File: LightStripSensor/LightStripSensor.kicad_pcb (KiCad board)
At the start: 2 copper layers, 61.8 x 40 mm, 14 parts, among them J1 LED_OUT 5.5x2.1, J2 DC_IN 12V 5.5x2.1, J3 HLK-LD2410B, Q1 IRLR7843, U1 ESP32-C3-SuperMini, U2 LM7805_TO220

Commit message: Update SCH/PCB
- Delete Mosfet and Zenner
- Design PCB
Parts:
- added D3: SMBJ15A, Diode_SMD:D_SMB, B.Cu at (113.6, 83.9)
- added F1: 7A fast, Fuse:Fuse_1812_4532Metric_Pad1.30x3.40mm_HandSolder, B.Cu at (105.0, 86.9)
- U2: value LM7805_TO220 -> L7805 (TO-263)
- moved U2 0.43 mm to (133.7, 93.7)
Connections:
- J2 pad 1: V_in -> Net-(F1-Pad1)
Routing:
- net VDD: track 31.7 -> 41.7 mm
- removed copper zone on B.Cu, net VDD

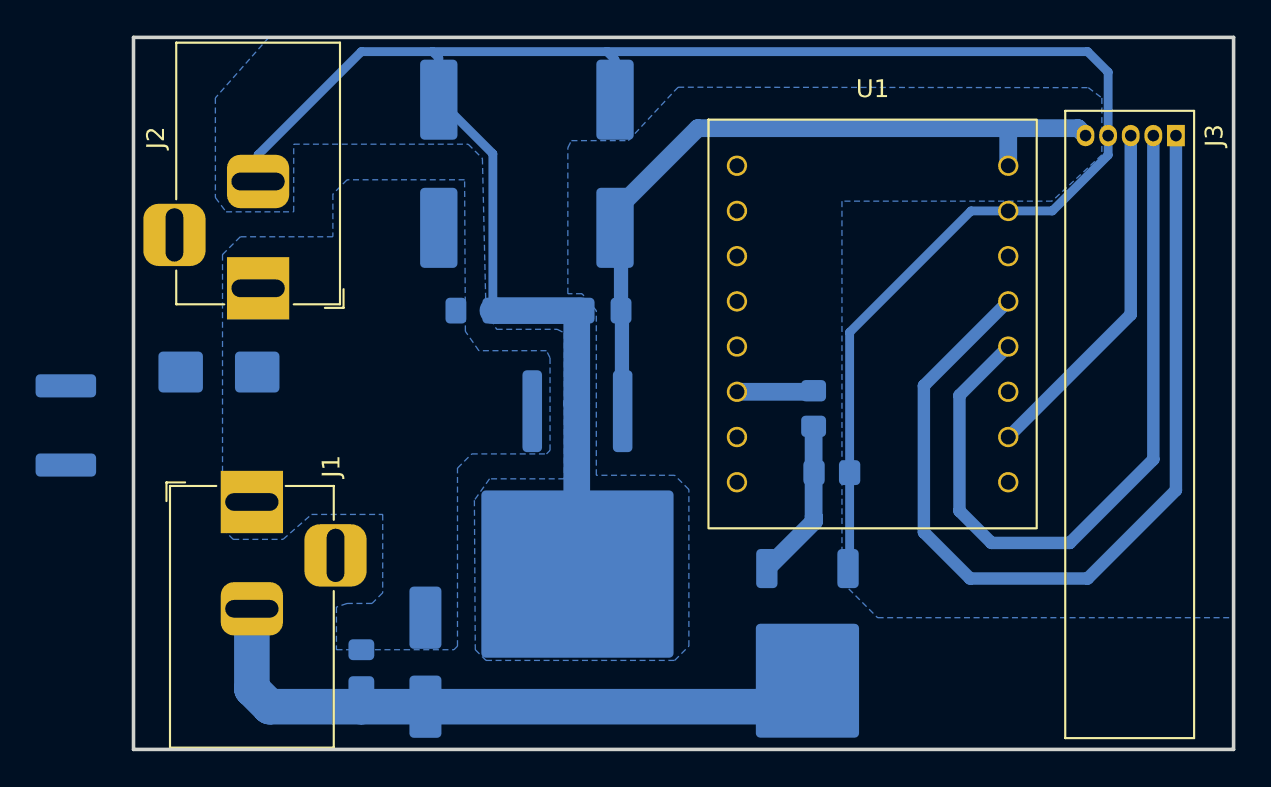
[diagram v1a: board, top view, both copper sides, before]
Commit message: Update Sch and PCB
- sch add capacitor  100nf
-  pcb redesign: Reroute
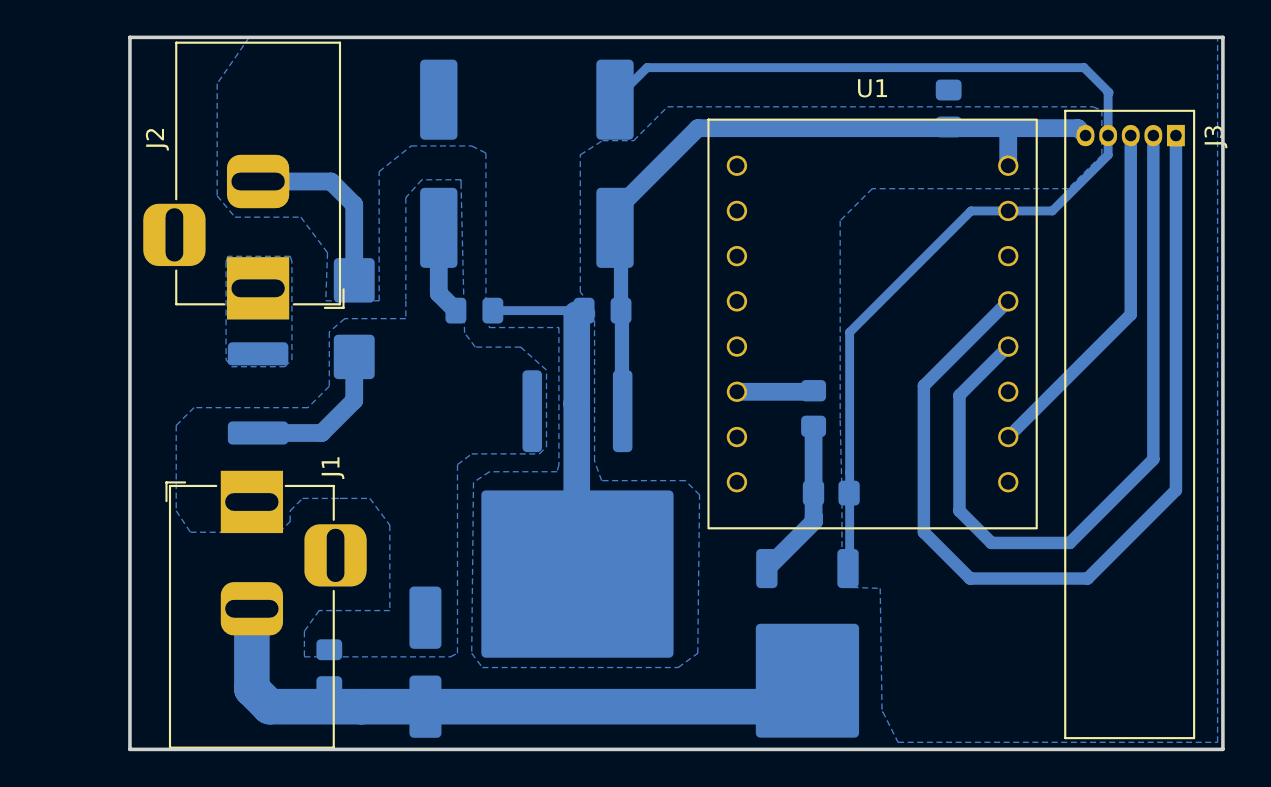
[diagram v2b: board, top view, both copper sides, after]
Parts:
- added C6: 100n, Capacitor_SMD:C_0805_2012Metric_Pad1.18x1.45mm_HandSolder, B.Cu at (154.6, 69.1)
- moved F1 10.9 mm to (115.8, 85.1), turned to -90 degrees
- moved D3 8.17 mm to (121.2, 80.9), turned to 90 degrees
- moved C1 1.80 mm to (119.8, 100.5)
- moved R1 1.15 mm to (148.0, 90.7)
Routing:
- net GND: track 127.0 -> 93.7 mm
- net V_in: track 0.00 -> 13.7 mm
- net Out1: track 37.9 -> 39.0 mm
- added copper zone on B.Cu, net Net-(F1-Pad1)
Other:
- board size 61.8 x 40 mm -> 61.4 x 40 mm
